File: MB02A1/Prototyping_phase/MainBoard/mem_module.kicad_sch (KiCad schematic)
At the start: 10 parts, among them U4 AMS1117-3.3, U5 W25Q64JVS, U6 25LC256, U7 25LC640

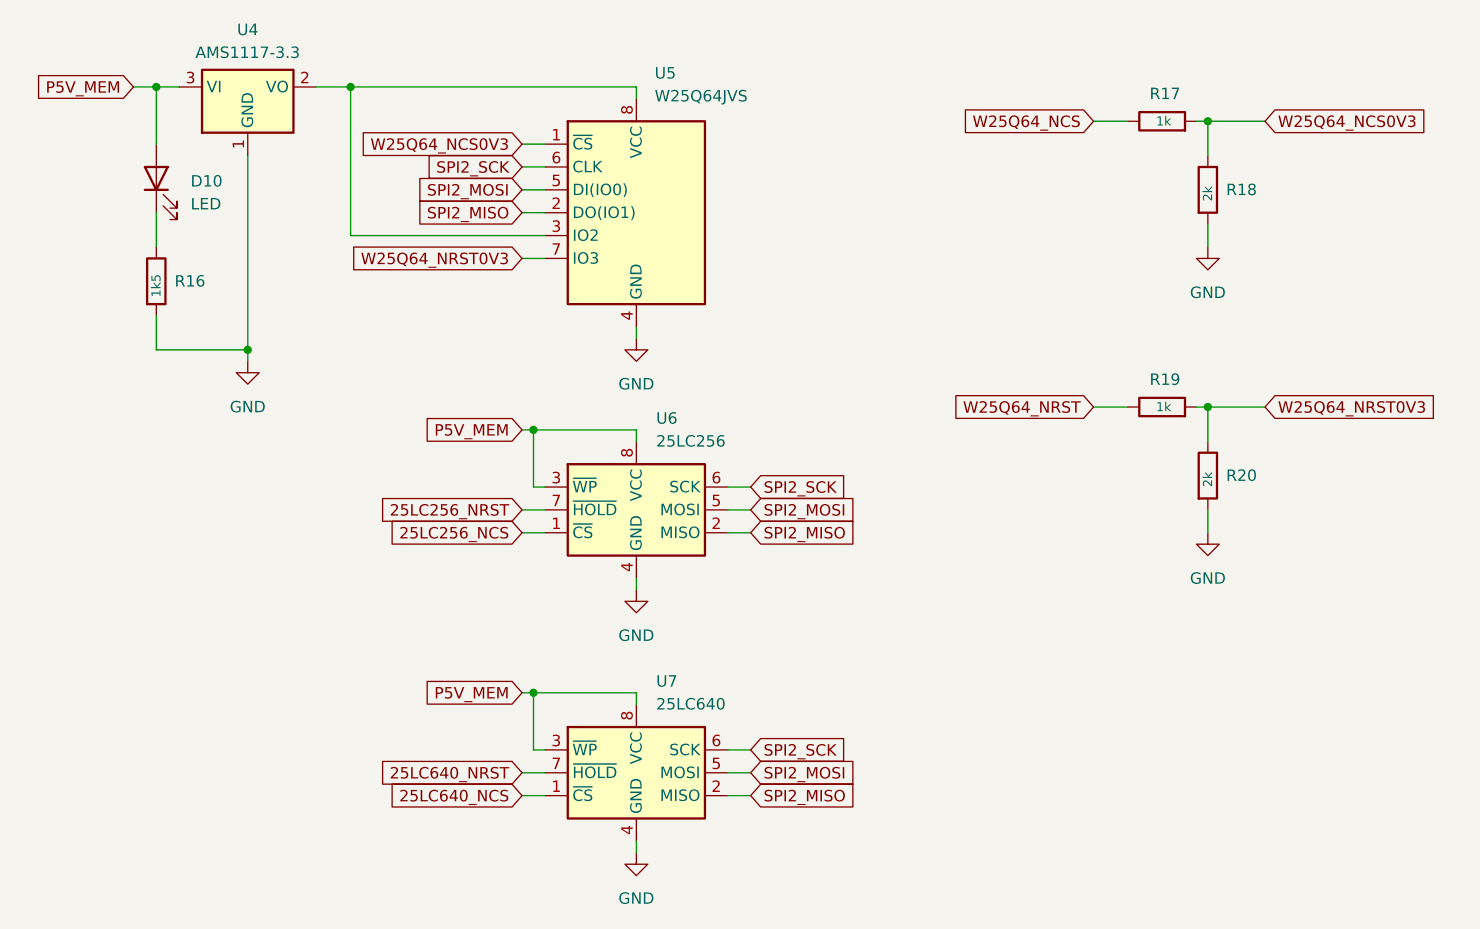
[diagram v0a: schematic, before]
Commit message: Datasheets added, design updated.
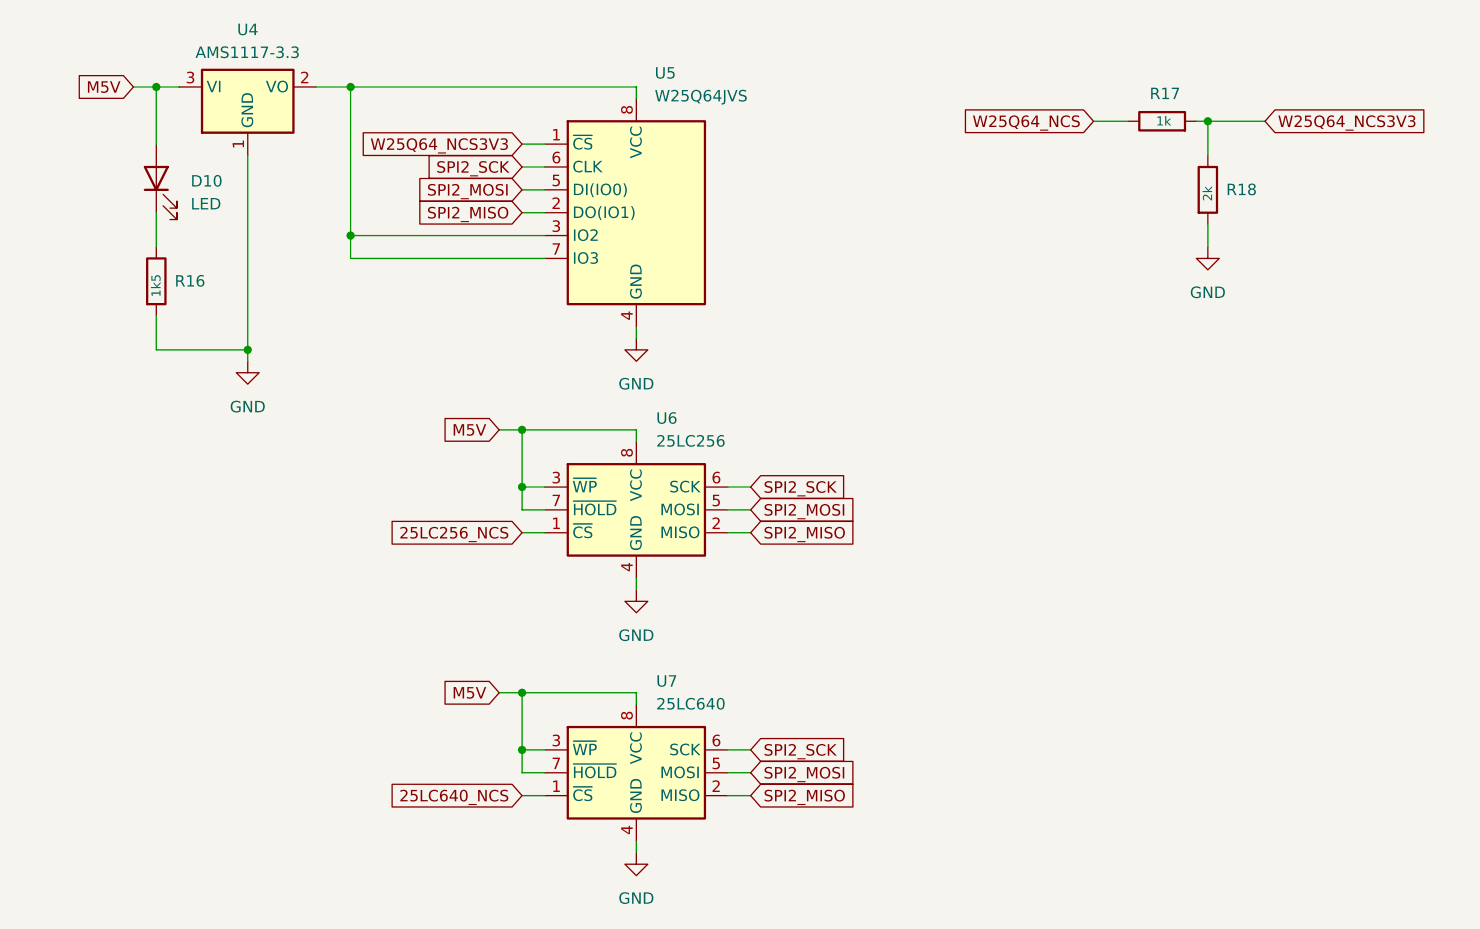
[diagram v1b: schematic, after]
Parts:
- removed R19: 1k, Resistor_SMD:R_0805_2012Metric, symbol Device:R
- removed R20: 2k, Resistor_SMD:R_0805_2012Metric, symbol Device:R
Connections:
- net 25LC640_NRST is gone; now on net M5V: U7.7 (~{HOLD})
- net P5V_MEM is gone; now on net M5V: D10.2 (A), U4.3 (VI), U6.3 (~{WP}), U6.8 (VCC), U7.3 (~{WP}), U7.8 (VCC)
- net W25Q64_NRST0V3 is gone; now on an unnamed net: U5.7 (IO3)
- net 25LC256_NRST renamed M5V
- net W25Q64_NCS0V3 renamed W25Q64_NCS3V3

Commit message: Design update, production preparation.
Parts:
- removed D10: LED, LED_SMD:LED_1206_3216Metric, symbol Device:LED
- removed R16: 1k5, Resistor_SMD:R_0805_2012Metric, symbol Device:R
- renumbered R17 to R20, R18 to R21, U4 to U5, U5 to U6, U6 to U7, U7 to U8
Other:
- title: MB02A1 - Memory Modul -> MB02A1 - Memory Module
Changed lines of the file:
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@@
 	(paper "A4")
 	(title_block
-		(title "MB02A1 - Memory Modul")
+		(title "MB02A1 - Memory Module")
 		(date "2025-01-18")
 		(rev "A1")
@@
 	)
 	(junction
-		(at 85.09 57.15)
-		(diameter 0)
-		(color 0 0 0 0)
-	)
-	(junction
 		(at 125.73 95.25)
 		(diameter 0)
@@
 	)
 	(junction
-		(at 95.25 86.36)
-		(diameter 0)
-		(color 0 0 0 0)
-	)
-	(junction
 		(at 106.68 57.15)
 		(diameter 0)
@@
 	(wire
 		(pts
-			(xy 82.55 57.15) (xy 85.09 57.15)
-		)
-		(stroke
-			(width 0)
-			(type default)
-		)
-	)
-	(wire
-		(pts
-			(xy 85.09 86.36) (xy 95.25 86.36)
+			(xy 82.55 57.15) (xy 87.63 57.15)
 		)
 		(stroke
@@
 	(wire
 		(pts
-			(xy 85.09 57.15) (xy 85.09 63.5)
-		)
-		(stroke
-			(width 0)
-			(type default)
-		)
-	)
-	(wire
-		(pts
 			(xy 106.68 57.15) (xy 138.43 57.15)
 		)
@@
 	(wire
 		(pts
-			(xy 95.25 86.36) (xy 95.25 87.63)
+			(xy 95.25 64.77) (xy 95.25 67.31)
 		)
 		(stroke
@@
 	(wire
 		(pts
-			(xy 95.25 64.77) (xy 95.25 86.36)
-		)
-		(stroke
-			(width 0)
-			(type default)
-		)
-	)
-	(wire
-		(pts
 			(xy 138.43 83.82) (xy 138.43 85.09)
 		)
@@
 	(wire
 		(pts
-			(xy 85.09 57.15) (xy 87.63 57.15)
-		)
-		(stroke
-			(width 0)
-			(type default)
-		)
-	)
-	(wire
-		(pts
 			(xy 125.73 124.46) (xy 138.43 124.46)
 		)
@@
 	(wire
 		(pts
-			(xy 85.09 82.55) (xy 85.09 86.36)
-		)
-		(stroke
-			(width 0)
-			(type default)
-		)
-	)
-	(wire
-		(pts
 			(xy 138.43 140.97) (xy 138.43 142.24)
 		)
@@
 		(pts
 			(xy 125.73 130.81) (xy 125.73 133.35)
-		)
-		(stroke
-			(width 0)
-			(type default)
-		)
-	)
-	(wire
-		(pts
-			(xy 85.09 71.12) (xy 85.09 74.93)
 		)
 		(stroke
@@
 		(dnp no)
 		(fields_autoplaced yes)
-		(property "Reference" "U6"
+		(property "Reference" "U7"
 			(at 140.6241 93.98 0)
 			(effects
@@
 			(project "mb02a1"
 				(path "/ee4e0941-1c36-4545-8b22-b979d73b3a97/b9c17cec-5b94-45c5-962d-af5c69f56587"
-					(reference "U6")
+					(reference "U7")
 					(unit 1)
 				)
@@
 		(dnp no)
 		(fields_autoplaced yes)
-		(property "Reference" "#PWR025"
+		(property "Reference" "#PWR026"
 			(at 138.43 148.59 0)
 			(effects
@@
 			(project "mb02a1"
 				(path "/ee4e0941-1c36-4545-8b22-b979d73b3a97/b9c17cec-5b94-45c5-962d-af5c69f56587"
-					(reference "#PWR025")
-					(unit 1)
-				)
-			)
-		)
-	)
-	(symbol
-		(lib_id "Device:LED")
-		(at 85.09 67.31 90)
-		(unit 1)
-		(exclude_from_sim no)
-		(in_bom yes)
-		(on_board yes)
-		(dnp no)
-		(fields_autoplaced yes)
-		(property "Reference" "D10"
-			(at 88.9 67.6274 90)
-			(effects
-				(font
-					(size 1.27 1.27)
-				)
-				(justify right)
-			)
-		)
-		(property "Value" "LED"
-			(at 88.9 70.1674 90)
-			(effects
-				(font
-					(size 1.27 1.27)
-				)
-				(justify right)
-			)
-		)
-		(property "Footprint" "LED_SMD:LED_1206_3216Metric"
-			(at 85.09 67.31 0)
-			(effects
-				(font
-					(size 1.27 1.27)
-				)
-				(hide yes)
-			)
-		)
-		(property "Datasheet" "~"
-			(at 85.09 67.31 0)
-			(effects
-				(font
-					(size 1.27 1.27)
-				)
-				(hide yes)
-			)
-		)
-		(property "Description" "Light emitting diode"
-			(at 85.09 67.31 0)
-			(effects
-				(font
-					(size 1.27 1.27)
-				)
-				(hide yes)
-			)
-		)
-		(pin "2"
-		)
-		(pin "1"
-		)
-		(instances
-			(project "mb02a1"
-				(path "/ee4e0941-1c36-4545-8b22-b979d73b3a97/b9c17cec-5b94-45c5-962d-af5c69f56587"
-					(reference "D10")
+					(reference "#PWR026")
 					(unit 1)
 				)
@@
 		(dnp no)
 		(fields_autoplaced yes)
-		(property "Reference" "U7"
+		(property "Reference" "U8"
 			(at 140.6241 123.19 0)
 			(effects
@@
 			(project "mb02a1"
 				(path "/ee4e0941-1c36-4545-8b22-b979d73b3a97/b9c17cec-5b94-45c5-962d-af5c69f56587"
-					(reference "U7")
+					(reference "U8")
 					(unit 1)
 				)
@@
 	(symbol
 		(lib_id "power:GND")
-		(at 95.25 87.63 0)
+		(at 95.25 67.31 0)
 		(unit 1)
 		(exclude_from_sim no)
@@
 		(dnp no)
 		(fields_autoplaced yes)
-		(property "Reference" "#PWR022"
-			(at 95.25 93.98 0)
+		(property "Reference" "#PWR023"
+			(at 95.25 73.66 0)
 			(effects
 				(font
@@
 		)
 		(property "Value" "GND"
-			(at 95.25 92.71 0)
+			(at 95.25 72.39 0)
 			(effects
 				(font
@@
 		)
 		(property "Footprint" ""
-			(at 95.25 87.63 0)
+			(at 95.25 67.31 0)
 			(effects
 				(font
@@
 		)
 		(property "Datasheet" ""
-			(at 95.25 87.63 0)
+			(at 95.25 67.31 0)
 			(effects
 				(font
@@
 		)
 		(property "Description" "Power symbol creates a global label with name \"GND\" , ground"
-			(at 95.25 87.63 0)
+			(at 95.25 67.31 0)
 			(effects
 				(font
@@
 			(project "mb02a1"
 				(path "/ee4e0941-1c36-4545-8b22-b979d73b3a97/b9c17cec-5b94-45c5-962d-af5c69f56587"
-					(reference "#PWR022")
-					(unit 1)
-				)
-			)
-		)
-	)
-	(symbol
-		(lib_id "Device:R")
-		(at 85.09 78.74 0)
-		(unit 1)
-		(exclude_from_sim no)
-		(in_bom yes)
-		(on_board yes)
-		(dnp no)
-		(property "Reference" "R16"
-			(at 87.122 78.74 0)
-			(effects
-				(font
-					(size 1.27 1.27)
-				)
-				(justify left)
-			)
-		)
-		(property "Value" "1k5"
-			(at 85.09 80.518 90)
-			(effects
-				(font
-					(size 1.016 1.016)
-				)
-				(justify left)
-			)
-		)
-		(property "Footprint" "Resistor_SMD:R_0805_2012Metric"
-			(at 83.312 78.74 90)
-			(effects
-				(font
-					(size 1.27 1.27)
-				)
-				(hide yes)
-			)
-		)
-		(property "Datasheet" "~"
-			(at 85.09 78.74 0)
-			(effects
-				(font
-					(size 1.27 1.27)
-				)
-				(hide yes)
-			)
-		)
-		(property "Description" "Resistor"
-			(at 85.09 78.74 0)
-			(effects
-				(font
-					(size 1.27 1.27)
-				)
-				(hide yes)
-			)
-		)
-		(pin "2"
-		)
-		(pin "1"
-		)
-		(instances
-			(project "mb02a1"
-				(path "/ee4e0941-1c36-4545-8b22-b979d73b3a97/b9c17cec-5b94-45c5-962d-af5c69f56587"
-					(reference "R16")
+					(reference "#PWR023")
 					(unit 1)
 				)
@@
 		(on_board yes)
 		(dnp no)
-		(property "Reference" "U5"
+		(property "Reference" "U6"
 			(at 140.462 55.626 0)
 			(effects
@@
 			(project "mb02a1"
 				(path "/ee4e0941-1c36-4545-8b22-b979d73b3a97/b9c17cec-5b94-45c5-962d-af5c69f56587"
-					(reference "U5")
+					(reference "U6")
 					(unit 1)
 				)
@@
 		(dnp no)
 		(fields_autoplaced yes)
-		(property "Reference" "#PWR023"
+		(property "Reference" "#PWR024"
 			(at 138.43 91.44 0)
 			(effects
@@
 			(project "mb02a1"
 				(path "/ee4e0941-1c36-4545-8b22-b979d73b3a97/b9c17cec-5b94-45c5-962d-af5c69f56587"
-					(reference "#PWR023")
+					(reference "#PWR024")
 					(unit 1)
 				)
@@
 		(dnp no)
 		(fields_autoplaced yes)
-		(property "Reference" "U4"
+		(property "Reference" "U5"
 			(at 95.25 50.8 0)
 			(effects
@@
 			(project "mb02a1"
 				(path "/ee4e0941-1c36-4545-8b22-b979d73b3a97/b9c17cec-5b94-45c5-962d-af5c69f56587"
-					(reference "U4")
+					(reference "U5")
 					(unit 1)
 				)
@@
 		(on_board yes)
 		(dnp no)
-		(property "Reference" "R18"
+		(property "Reference" "R21"
 			(at 203.962 68.58 0)
 			(effects
@@
 			(project "mb02a1"
 				(path "/ee4e0941-1c36-4545-8b22-b979d73b3a97/b9c17cec-5b94-45c5-962d-af5c69f56587"
-					(reference "R18")
+					(reference "R21")
 					(unit 1)
 				)
@@
 		(dnp no)
 		(fields_autoplaced yes)
-		(property "Reference" "#PWR026"
+		(property "Reference" "#PWR027"
 			(at 201.93 81.28 0)
 			(effects
@@
 			(project "mb02a1"
 				(path "/ee4e0941-1c36-4545-8b22-b979d73b3a97/b9c17cec-5b94-45c5-962d-af5c69f56587"
-					(reference "#PWR026")
+					(reference "#PWR027")
 					(unit 1)
 				)
@@
 		(dnp no)
 		(fields_autoplaced yes)
-		(property "Reference" "#PWR024"
+		(property "Reference" "#PWR025"
 			(at 138.43 119.38 0)
 			(effects
@@
 			(project "mb02a1"
 				(path "/ee4e0941-1c36-4545-8b22-b979d73b3a97/b9c17cec-5b94-45c5-962d-af5c69f56587"
-					(reference "#PWR024")
+					(reference "#PWR025")
 					(unit 1)
 				)
@@
 		(on_board yes)
 		(dnp no)
-		(property "Reference" "R17"
+		(property "Reference" "R20"
 			(at 198.882 57.912 90)
 			(effects
@@
 			(project "mb02a1"
 				(path "/ee4e0941-1c36-4545-8b22-b979d73b3a97/b9c17cec-5b94-45c5-962d-af5c69f56587"
-					(reference "R17")
+					(reference "R20")
 					(unit 1)
 				)
